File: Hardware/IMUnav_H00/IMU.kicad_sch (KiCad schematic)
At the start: 28 parts, among them U11 MPU-6050, U12 LSM303AGR, U13 ADIS16505-2BMLZ, U14 ADIS16505-x/PCBZ

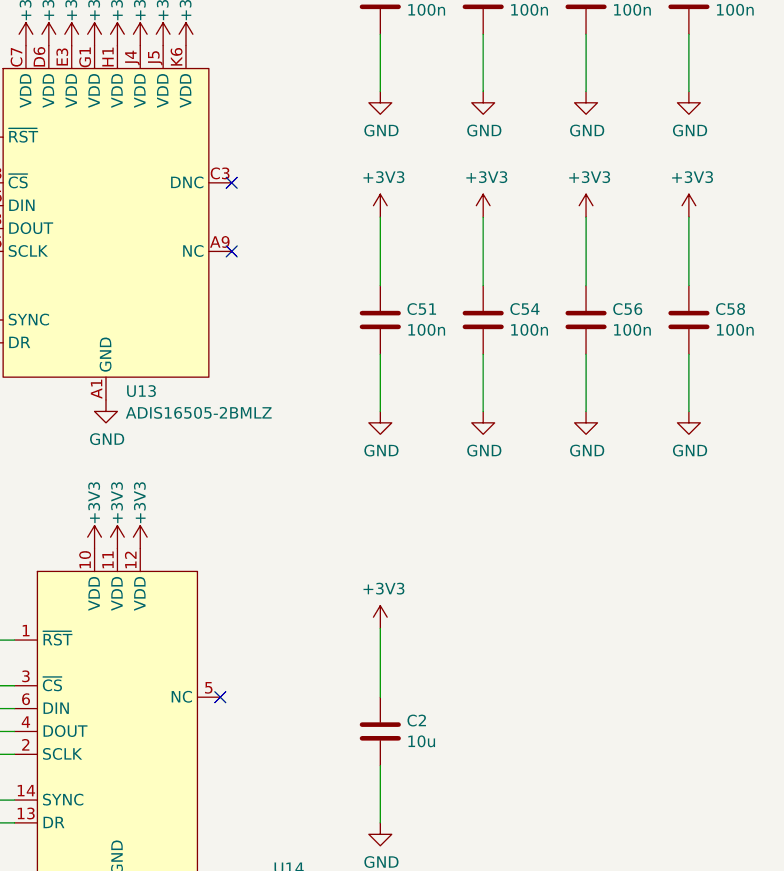
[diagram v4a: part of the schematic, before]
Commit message: PCB layout - BGA fanout, GPS and USB hub
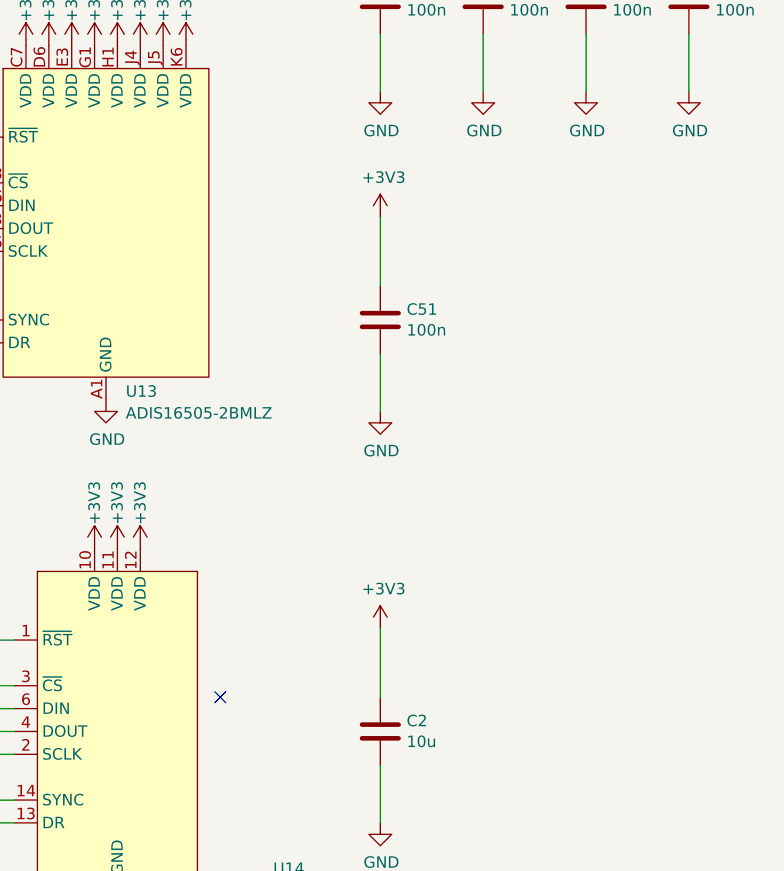
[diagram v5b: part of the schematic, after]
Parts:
- removed C54, C56, C58: 100n, Capacitor_SMD:C_0603_1608Metric, symbol Device:C
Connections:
- now unconnected: U13.A10 (NC), U13.A9 (NC), U13.B1 (NC), U13.B10 (NC), U13.B2 (NC), U13.B7 (NC), U13.B8 (NC), U13.B9 (NC), U13.C1 (NC), U13.C10 (NC), U13.C4 (NC), U13.C5 (NC), U13.C8 (NC), U13.C9 (NC), U13.D1 (NC), U13.D10 (NC), U13.D2 (NC), U13.D4 (NC), U13.D5 (NC), U13.D7 (NC), U13.D8 (NC), U13.D9 (NC), U13.E1 (NC), U13.E10 (NC), U13.E4 (NC), U13.E5 (NC), U13.E8 (NC), U13.E9 (NC), U13.F10 (NC), U13.F2 (NC), U13.F4 (NC), U13.F7 (NC), U13.F9 (NC), U13.G10 (NC), U13.G4 (NC), U13.G5 (NC), U13.G8 (NC), U13.G9 (NC), U13.H10 (NC), U13.H2 (NC), U13.H4 (NC), U13.H5 (NC), U13.H7 (NC), U13.H9 (NC), U13.J1 (NC), U13.J10 (NC), U13.J8 (NC), U13.J9 (NC), U13.K10 (NC), U13.K2 (NC), U13.K4 (NC), U13.K5 (NC), U13.K7 (NC), U13.K9 (NC), U14.15 (NC), U14.16 (NC), U14.5 (NC)
- no-connect marks 5 -> 3

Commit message: PCB routing
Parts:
- C50, C51, C53, C55, C57, U13: now not fitted
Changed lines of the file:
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@@
     (stroke (width 0) (type default))
   )
-  (wire (pts (xy 245.11 62.23) (xy 245.11 68.58))
+  (wire (pts (xy 222.25 97.79) (xy 222.25 104.14))
     (stroke (width 0) (type default))
   )
@@
     (stroke (width 0) (type default))
   )
-  (wire (pts (xy 245.11 46.99) (xy 245.11 54.61))
+  (wire (pts (xy 222.25 82.55) (xy 222.25 90.17))
     (stroke (width 0) (type default))
   )
@@
   )
   (symbol (lib_id "Device:C") (at 233.68 58.42 0) (unit 1)
-    (in_bom yes) (on_board yes) (dnp no)
+    (in_bom yes) (on_board yes) (dnp yes)
     (property "Reference" "C55" (at 236.601 57.2516 0)
       (effects (font (size 1.27 1.27)) (justify left))
@@
   )
   (symbol (lib_id "IMUnav:ADIS16505") (at 180.34 85.09 0) (unit 1)
-    (in_bom yes) (on_board yes) (dnp no) (fields_autoplaced)
+    (in_bom yes) (on_board yes) (dnp yes) (fields_autoplaced)
     (property "Reference" "U13" (at 182.5341 101.9231 0)
       (effects (font (size 1.27 1.27)) (justify left))
@@
     )
   )
-  (symbol (lib_id "power:+3V3") (at 245.11 46.99 0) (unit 1)
-    (in_bom yes) (on_board yes) (dnp no)
-    (property "Reference" "#PWR0183" (at 245.11 50.8 0)
-      (effects (font (size 1.27 1.27)) hide)
-    )
-    (property "Value" "+3V3" (at 245.491 42.5958 0)
-      (effects (font (size 1.27 1.27)))
-    )
-    (property "Footprint" "" (at 245.11 46.99 0)
-      (effects (font (size 1.27 1.27)) hide)
-    )
-    (property "Datasheet" "" (at 245.11 46.99 0)
+  (symbol (lib_id "power:+3V3") (at 222.25 82.55 0) (unit 1)
+    (in_bom yes) (on_board yes) (dnp no)
+    (property "Reference" "#PWR0183" (at 222.25 86.36 0)
+      (effects (font (size 1.27 1.27)) hide)
+    )
+    (property "Value" "+3V3" (at 222.631 78.1558 0)
+      (effects (font (size 1.27 1.27)))
+    )
+    (property "Footprint" "" (at 222.25 82.55 0)
+      (effects (font (size 1.27 1.27)) hide)
+    )
+    (property "Datasheet" "" (at 222.25 82.55 0)
       (effects (font (size 1.27 1.27)) hide)
     )
@@
   )
   (symbol (lib_id "Device:C") (at 210.82 93.98 0) (unit 1)
-    (in_bom yes) (on_board yes) (dnp no)
+    (in_bom yes) (on_board yes) (dnp yes)
     (property "Reference" "C51" (at 213.741 92.8116 0)
       (effects (font (size 1.27 1.27)) (justify left))
@@
   )
   (symbol (lib_id "Device:C") (at 222.25 58.42 0) (unit 1)
-    (in_bom yes) (on_board yes) (dnp no)
+    (in_bom yes) (on_board yes) (dnp yes)
     (property "Reference" "C53" (at 225.171 57.2516 0)
       (effects (font (size 1.27 1.27)) (justify left))
@@
   )
   (symbol (lib_id "Device:C") (at 210.82 58.42 0) (unit 1)
-    (in_bom yes) (on_board yes) (dnp no)
+    (in_bom yes) (on_board yes) (dnp yes)
     (property "Reference" "C50" (at 213.741 57.2516 0)
       (effects (font (size 1.27 1.27)) (justify left))
@@
     )
   )
-  (symbol (lib_id "power:GND") (at 245.11 68.58 0) (unit 1)
-    (in_bom yes) (on_board yes) (dnp no)
-    (property "Reference" "#PWR0184" (at 245.11 74.93 0)
-      (effects (font (size 1.27 1.27)) hide)
-    )
-    (property "Value" "GND" (at 245.237 72.9742 0)
-      (effects (font (size 1.27 1.27)))
-    )
-    (property "Footprint" "" (at 245.11 68.58 0)
-      (effects (font (size 1.27 1.27)) hide)
-    )
-    (property "Datasheet" "" (at 245.11 68.58 0)
+  (symbol (lib_id "power:GND") (at 222.25 104.14 0) (unit 1)
+    (in_bom yes) (on_board yes) (dnp no)
+    (property "Reference" "#PWR0184" (at 222.25 110.49 0)
+      (effects (font (size 1.27 1.27)) hide)
+    )
+    (property "Value" "GND" (at 222.377 108.5342 0)
+      (effects (font (size 1.27 1.27)))
+    )
+    (property "Footprint" "" (at 222.25 104.14 0)
+      (effects (font (size 1.27 1.27)) hide)
+    )
+    (property "Datasheet" "" (at 222.25 104.14 0)
       (effects (font (size 1.27 1.27)) hide)
     )
@@
     )
   )
-  (symbol (lib_id "Device:C") (at 245.11 58.42 0) (unit 1)
-    (in_bom yes) (on_board yes) (dnp no)
-    (property "Reference" "C57" (at 248.031 57.2516 0)
-      (effects (font (size 1.27 1.27)) (justify left))
-    )
-    (property "Value" "100n" (at 248.031 59.563 0)
-      (effects (font (size 1.27 1.27)) (justify left))
-    )
-    (property "Footprint" "Capacitor_SMD:C_0603_1608Metric" (at 246.0752 62.23 0)
-      (effects (font (size 1.27 1.27)) hide)
-    )
-    (property "Datasheet" "~" (at 245.11 58.42 0)
-      (effects (font (size 1.27 1.27)) hide)
-    )
-    (property "LCSC" "C14663" (at 245.11 58.42 0)
-      (effects (font (size 1.27 1.27)) hide)
-    )
+  (symbol (lib_id "Device:C") (at 222.25 93.98 0) (unit 1)
+    (in_bom yes) (on_board yes) (dnp yes)
+    (property "Reference" "C57" (at 225.171 92.8116 0)
+      (effects (font (size 1.27 1.27)) (justify left))
+    )
+    (property "Value" "100n" (at 225.171 95.123 0)
+      (effects (font (size 1.27 1.27)) (justify left))
+    )
+    (property "Footprint" "Capacitor_SMD:C_0603_1608Metric" (at 223.2152 97.79 0)
+      (effects (font (size 1.27 1.27)) hide)
+    )
+    (property "Datasheet" "~" (at 222.25 93.98 0)
+      (effects (font (size 1.27 1.27)) hide)
+    )
+    (property "LCSC" "C14663" (at 222.25 93.98 0)
+      (effects (font (size 1.27 1.27)) hide)
+    )

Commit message: Silkscreen layout
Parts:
- renumbered C57 to C54

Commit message: Thesis - added appendix
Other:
- note added: "ADIS16505 - accel + gyro BGA and PCB version"
- note added: "ALSM3030 - accel + magnetometer"
- note added: "MPU6050 - accel + gyro"
- title: (none) -> IMUnav
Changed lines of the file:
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@@
 (kicad_sch (version 20230121) (generator eeschema)
   (paper "A4")
+  (title_block
+    (title "IMUnav")
+    (date "2023-12-21")
+    (rev "H00")
+    (comment 1 "Inertial navigation unit")
+  )
   (junction (at 157.48 96.52) (diameter 0) (color 0 0 0 0)
   )
@@
     (stroke (width 0) (type default))
   )
+  (text "ADIS16505 - accel + gyro\nBGA and PCB version" (at 168.91 33.02 0)
+    (effects (font (size 2.54 2.54) (thickness 0.508) bold) (justify left bottom))
+  )
+  (text "MPU6050 - accel + gyro" (at 59.69 19.05 0)
+    (effects (font (size 2.54 2.54) (thickness 0.508) bold) (justify left bottom))
+  )
+  (text "ALSM3030 - accel + magnetometer" (at 45.72 86.36 0)
+    (effects (font (size 2.54 2.54) (thickness 0.508) bold) (justify left bottom))
+  )
   (hierarchical_label "ADIS_~{CS}" (shape input) (at 140.97 78.74 180) (fields_autoplaced)
